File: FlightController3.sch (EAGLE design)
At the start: 43 parts, among them U1 NUCLEO_L432KC

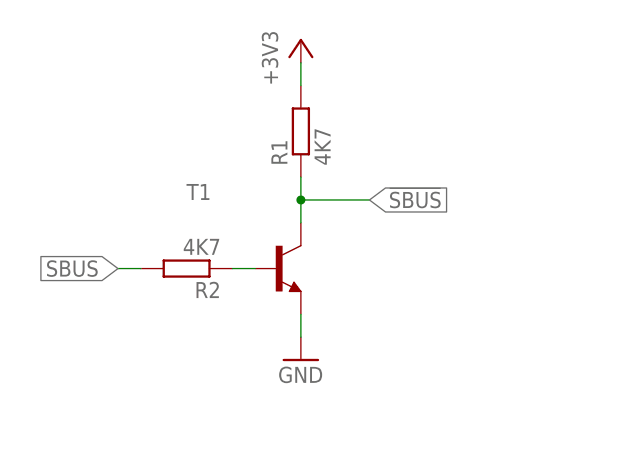
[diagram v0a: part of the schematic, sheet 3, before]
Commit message: sbus inverter spice setup
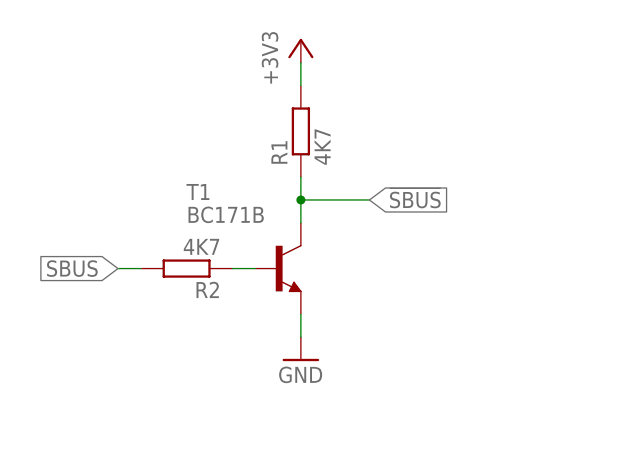
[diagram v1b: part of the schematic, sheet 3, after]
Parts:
- MF1: SPICEPREFIX (none) -> X
- R1, R2: SPICEPREFIX (none) -> R
- T1: value (none) -> BC171B; SPICEMODEL (none) -> BC171B; SPICEPREFIX (none) -> Q
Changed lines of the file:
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@@
 <part name="P+2" library="supply1" library_urn="urn:adsk.eagle:library:371" deviceset="+5V" device=""/>
 <part name="GND3" library="supply1" library_urn="urn:adsk.eagle:library:371" deviceset="GND" device=""/>
-<part name="T1" library="transistor" library_urn="urn:adsk.eagle:library:402" deviceset="*-NPN-" device="TO92"/>
-<part name="R1" library="resistor" library_urn="urn:adsk.eagle:library:348" deviceset="R-EU_" device="R0603" value="4K7"/>
-<part name="R2" library="resistor" library_urn="urn:adsk.eagle:library:348" deviceset="R-EU_" device="R0603" value="4K7"/>
+<part name="T1" library="transistor" library_urn="urn:adsk.eagle:library:402" deviceset="*-NPN-" device="TO92" value="BC171B">
+<spice>
+<pinmapping isusermap="yes" isdevicewide="no">
+<pinmap gate="G$1" pin="B" pinorder="2"/>
+<pinmap gate="G$1" pin="E" pinorder="3"/>
+<pinmap gate="G$1" pin="C" pinorder="1"/>
+</pinmapping>
+</spice>
+<attribute name="SPICEMODEL" value="BC171B"/>
+<attribute name="SPICEPREFIX" value="Q"/>
+</part>
+<part name="R1" library="resistor" library_urn="urn:adsk.eagle:library:348" deviceset="R-EU_" device="R0603" value="4K7">
+<spice>
+<pinmapping isusermap="yes" isdevicewide="yes">
+<pinmap gate="G$1" pin="2" pinorder="1"/>
+<pinmap gate="G$1" pin="1" pinorder="2"/>
+</pinmapping>
+</spice>
+<attribute name="SPICEPREFIX" value="R"/>
+</part>
+<part name="R2" library="resistor" library_urn="urn:adsk.eagle:library:348" deviceset="R-EU_" device="R0603" value="4K7">
+<spice>
+<pinmapping isusermap="yes" isdevicewide="yes">
+<pinmap gate="G$1" pin="2" pinorder="1"/>
+<pinmap gate="G$1" pin="1" pinorder="2"/>
+</pinmapping>
+</spice>
+<attribute name="SPICEPREFIX" value="R"/>
+</part>
 <part name="+3V3" library="supply1" library_urn="urn:adsk.eagle:library:371" deviceset="+3V3" device=""/>
 <part name="GND6" library="supply1" library_urn="urn:adsk.eagle:library:371" deviceset="GND" device=""/>
 <part name="INS1" library="1_Robo-Lib" deviceset="BNO055-BREAKOUT" device="" value="BNO055"/>
 <part name="GND7" library="supply1" library_urn="urn:adsk.eagle:library:371" deviceset="GND" device=""/>
-<part name="MF1" library="BSN20_215" deviceset="BSN20,215" device=""/>
+<part name="MF1" library="BSN20_215" deviceset="BSN20,215" device="">
+<attribute name="SPICEPREFIX" value="X"/>
+</part>
 <part name="MF2" library="BSN20_215" deviceset="BSN20,215" device=""/>
 <part name="R3" library="resistor" library_urn="urn:adsk.eagle:library:348" deviceset="R-EU_" device="R0603" value="4K7"/>
@@
 with this version.
 </note>
+<note version="8.4" severity="warning">
+Since Version 8.4, EAGLE supports properties for SPICE simulation.
+Probes in schematics and SPICE mapping objects found in parts and library devices
+will not be understood with this version. Update EAGLE to the latest version
+for full support of SPICE simulation.
+</note>
 </compatibility>

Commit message: i2c level shifting simulation setup
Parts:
- MF1: SPICEMODEL (none) -> BSN20
- MF2: SPICEMODEL (none) -> BSN20; SPICEPREFIX (none) -> X
- R3, R4, R5, R6: SPICEPREFIX (none) -> R
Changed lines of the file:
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@@
 <part name="GND7" library="supply1" library_urn="urn:adsk.eagle:library:371" deviceset="GND" device=""/>
 <part name="MF1" library="BSN20_215" deviceset="BSN20,215" device="">
+<spice>
+<pinmapping isusermap="yes" isdevicewide="no">
+<pinmap gate="G$1" pin="D" pinorder="1"/>
+<pinmap gate="G$1" pin="S" pinorder="3"/>
+<pinmap gate="G$1" pin="G" pinorder="2"/>
+</pinmapping>
+</spice>
+<attribute name="SPICEMODEL" value="BSN20"/>
 <attribute name="SPICEPREFIX" value="X"/>
 </part>
-<part name="MF2" library="BSN20_215" deviceset="BSN20,215" device=""/>
-<part name="R3" library="resistor" library_urn="urn:adsk.eagle:library:348" deviceset="R-EU_" device="R0603" value="4K7"/>
-<part name="R4" library="resistor" library_urn="urn:adsk.eagle:library:348" deviceset="R-EU_" device="R0603" value="4K7"/>
-<part name="R5" library="resistor" library_urn="urn:adsk.eagle:library:348" deviceset="R-EU_" device="R0603" value="4K7"/>
-<part name="R6" library="resistor" library_urn="urn:adsk.eagle:library:348" deviceset="R-EU_" device="R0603" value="4K7"/>
+<part name="MF2" library="BSN20_215" deviceset="BSN20,215" device="">
+<spice>
+<pinmapping isusermap="yes" isdevicewide="no">
+<pinmap gate="G$1" pin="D" pinorder="1"/>
+<pinmap gate="G$1" pin="S" pinorder="3"/>
+<pinmap gate="G$1" pin="G" pinorder="2"/>
+</pinmapping>
+</spice>
+<attribute name="SPICEMODEL" value="BSN20"/>
+<attribute name="SPICEPREFIX" value="X"/>
+</part>
+<part name="R3" library="resistor" library_urn="urn:adsk.eagle:library:348" deviceset="R-EU_" device="R0603" value="4K7">
+<spice>
+<pinmapping isusermap="yes" isdevicewide="yes">
+<pinmap gate="G$1" pin="2" pinorder="1"/>
+<pinmap gate="G$1" pin="1" pinorder="2"/>
+</pinmapping>
+</spice>
+<attribute name="SPICEPREFIX" value="R"/>
+</part>
+<part name="R4" library="resistor" library_urn="urn:adsk.eagle:library:348" deviceset="R-EU_" device="R0603" value="4K7">
+<spice>
+<pinmapping isusermap="yes" isdevicewide="yes">
+<pinmap gate="G$1" pin="2" pinorder="1"/>
+<pinmap gate="G$1" pin="1" pinorder="2"/>
+</pinmapping>
+</spice>
+<attribute name="SPICEPREFIX" value="R"/>
+</part>
+<part name="R5" library="resistor" library_urn="urn:adsk.eagle:library:348" deviceset="R-EU_" device="R0603" value="4K7">
+<spice>
+<pinmapping isusermap="yes" isdevicewide="yes">
+<pinmap gate="G$1" pin="2" pinorder="1"/>
+<pinmap gate="G$1" pin="1" pinorder="2"/>
+</pinmapping>
+</spice>
+<attribute name="SPICEPREFIX" value="R"/>
+</part>
+<part name="R6" library="resistor" library_urn="urn:adsk.eagle:library:348" deviceset="R-EU_" device="R0603" value="4K7">
+<spice>
+<pinmapping isusermap="yes" isdevicewide="yes">
+<pinmap gate="G$1" pin="2" pinorder="1"/>
+<pinmap gate="G$1" pin="1" pinorder="2"/>
+</pinmapping>
+</spice>
+<attribute name="SPICEPREFIX" value="R"/>
+</part>
 <part name="+3V5" library="supply1" library_urn="urn:adsk.eagle:library:371" deviceset="+3V3" device=""/>
 <part name="P+4" library="supply1" library_urn="urn:adsk.eagle:library:371" deviceset="+5V" device=""/>

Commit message: power led simulation setup
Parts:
- LED1, LED2: SPICEMODEL (none) -> SMLD12U8W; SPICEPREFIX (none) -> D
- R7, R8: SPICEPREFIX (none) -> R
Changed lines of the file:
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@@
 <part name="JP1" library="pinhead" library_urn="urn:adsk.eagle:library:325" deviceset="PINHD-1X2" device="" value="RESET"/>
 <part name="GND8" library="supply1" library_urn="urn:adsk.eagle:library:371" deviceset="GND" device=""/>
-<part name="LED1" library="led" library_urn="urn:adsk.eagle:library:259" deviceset="LED" device="SML0603" value="5V"/>
-<part name="LED2" library="led" library_urn="urn:adsk.eagle:library:259" deviceset="LED" device="SML0603" value="3V3"/>
+<part name="LED1" library="led" library_urn="urn:adsk.eagle:library:259" deviceset="LED" device="SML0603" value="5V">
+<spice>
+<pinmapping isusermap="yes" isdevicewide="no">
+<pinmap gate="G$1" pin="A" pinorder="1"/>
+<pinmap gate="G$1" pin="C" pinorder="2"/>
+</pinmapping>
+</spice>
+<attribute name="SPICEMODEL" value="SMLD12U8W"/>
+<attribute name="SPICEPREFIX" value="D"/>
+</part>
+<part name="LED2" library="led" library_urn="urn:adsk.eagle:library:259" deviceset="LED" device="SML0603" value="3V3">
+<spice>
+<pinmapping isusermap="yes" isdevicewide="no">
+<pinmap gate="G$1" pin="A" pinorder="1"/>
+<pinmap gate="G$1" pin="C" pinorder="2"/>
+</pinmapping>
+</spice>
+<attribute name="SPICEMODEL" value="SMLD12U8W"/>
+<attribute name="SPICEPREFIX" value="D"/>
+</part>
 <part name="+3V2" library="supply1" library_urn="urn:adsk.eagle:library:371" deviceset="+3V3" device=""/>
 <part name="P+8" library="supply1" library_urn="urn:adsk.eagle:library:371" deviceset="+5V" device=""/>
-<part name="R7" library="resistor" library_urn="urn:adsk.eagle:library:348" deviceset="R-EU_" device="M1206" value="110"/>
-<part name="R8" library="resistor" library_urn="urn:adsk.eagle:library:348" deviceset="R-EU_" device="M1206" value="150"/>
+<part name="R7" library="resistor" library_urn="urn:adsk.eagle:library:348" deviceset="R-EU_" device="M1206" value="110">
+<spice>
+<pinmapping isusermap="yes" isdevicewide="yes">
+<pinmap gate="G$1" pin="2" pinorder="1"/>
+<pinmap gate="G$1" pin="1" pinorder="2"/>
+</pinmapping>
+</spice>
+<attribute name="SPICEPREFIX" value="R"/>
+</part>
+<part name="R8" library="resistor" library_urn="urn:adsk.eagle:library:348" deviceset="R-EU_" device="M1206" value="150">
+<spice>
+<pinmapping isusermap="yes" isdevicewide="yes">
+<pinmap gate="G$1" pin="2" pinorder="1"/>
+<pinmap gate="G$1" pin="1" pinorder="2"/>
+</pinmapping>
+</spice>
+<attribute name="SPICEPREFIX" value="R"/>
+</part>
 <part name="GND9" library="supply1" library_urn="urn:adsk.eagle:library:371" deviceset="GND" device=""/>
 <part name="GND10" library="supply1" library_urn="urn:adsk.eagle:library:371" deviceset="GND" device=""/>

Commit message: filtering capacitor simulation setup
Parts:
- C15, C16, C17, C18: SPICEPREFIX (none) -> C
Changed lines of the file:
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@@
 <part name="GND9" library="supply1" library_urn="urn:adsk.eagle:library:371" deviceset="GND" device=""/>
 <part name="GND10" library="supply1" library_urn="urn:adsk.eagle:library:371" deviceset="GND" device=""/>
-<part name="C15" library="resistor" library_urn="urn:adsk.eagle:library:348" deviceset="C-EU" device="C1206" value="100nF"/>
-<part name="C16" library="resistor" library_urn="urn:adsk.eagle:library:348" deviceset="C-EU" device="C1206" value="100nF"/>
-<part name="C17" library="resistor" library_urn="urn:adsk.eagle:library:348" deviceset="C-EU" device="C1206" value="100nF"/>
-<part name="C18" library="resistor" library_urn="urn:adsk.eagle:library:348" deviceset="C-EU" device="C1206" value="100nF"/>
+<part name="C15" library="resistor" library_urn="urn:adsk.eagle:library:348" deviceset="C-EU" device="C1206" value="100nF">
+<spice>
+<pinmapping isusermap="yes" isdevicewide="yes">
+<pinmap gate="G$1" pin="2" pinorder="2"/>
+<pinmap gate="G$1" pin="1" pinorder="1"/>
+</pinmapping>
+</spice>
+<attribute name="SPICEPREFIX" value="C"/>
+</part>
+<part name="C16" library="resistor" library_urn="urn:adsk.eagle:library:348" deviceset="C-EU" device="C1206" value="100nF">
+<spice>
+<pinmapping isusermap="yes" isdevicewide="yes">
+<pinmap gate="G$1" pin="2" pinorder="2"/>
+<pinmap gate="G$1" pin="1" pinorder="1"/>
+</pinmapping>
+</spice>
+<attribute name="SPICEPREFIX" value="C"/>
+</part>
+<part name="C17" library="resistor" library_urn="urn:adsk.eagle:library:348" deviceset="C-EU" device="C1206" value="100nF">
+<spice>
+<pinmapping isusermap="yes" isdevicewide="yes">
+<pinmap gate="G$1" pin="2" pinorder="2"/>
+<pinmap gate="G$1" pin="1" pinorder="1"/>
+</pinmapping>
+</spice>
+<attribute name="SPICEPREFIX" value="C"/>
+</part>
+<part name="C18" library="resistor" library_urn="urn:adsk.eagle:library:348" deviceset="C-EU" device="C1206" value="100nF">
+<spice>
+<pinmapping isusermap="yes" isdevicewide="yes">
+<pinmap gate="G$1" pin="2" pinorder="2"/>
+<pinmap gate="G$1" pin="1" pinorder="1"/>
+</pinmapping>
+</spice>
+<attribute name="SPICEPREFIX" value="C"/>
+</part>
 <part name="P+10" library="supply1" library_urn="urn:adsk.eagle:library:371" deviceset="+5V" device=""/>
 <part name="P+11" library="supply1" library_urn="urn:adsk.eagle:library:371" deviceset="+5V" device=""/>

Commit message: nucleo simulation setup
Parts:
- U1: SPICEMODEL (none) -> NUCLEO; SPICEPREFIX (none) -> X
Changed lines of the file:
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@@
 <part name="+3V5" library="supply1" library_urn="urn:adsk.eagle:library:371" deviceset="+3V3" device=""/>
 <part name="P+4" library="supply1" library_urn="urn:adsk.eagle:library:371" deviceset="+5V" device=""/>
-<part name="U1" library="NUCLEO" deviceset="NUCLEO_L432KC" device=""/>
+<part name="U1" library="NUCLEO" deviceset="NUCLEO_L432KC" device="">
+<spice>
+<pinmapping isusermap="yes" isdevicewide="no">
+<pinmap gate="G$1" pin="D3" pinorder="4"/>
+<pinmap gate="G$1" pin="A3" pinorder="16"/>
+<pinmap gate="G$1" pin="D6" pinorder="7"/>
+<pinmap gate="G$1" pin="D12/SDA3" pinorder="11"/>
+<pinmap gate="G$1" pin="VIN" pinorder="21"/>
+<pinmap gate="G$1" pin="A5" pinorder="18"/>
+<pinmap gate="G$1" pin="A6/SCL3" pinorder="19"/>
+<pinmap gate="G$1" pin="!RST" pinorder="26"/>
+<pinmap gate="G$1" pin="A1" pinorder="14"/>
+<pinmap gate="G$1" pin="D0/SCL1/RX1" pinorder="1"/>
+<pinmap gate="G$1" pin="D2" pinorder="3"/>
+<pinmap gate="G$1" pin="GND" pinorder="22"/>
+<pinmap gate="G$1" pin="A4" pinorder="17"/>
+<pinmap gate="G$1" pin="D13" pinorder="12"/>
+<pinmap gate="G$1" pin="+5V" pinorder="23"/>
+<pinmap gate="G$1" pin="D1/SDA1/TX1" pinorder="2"/>
+<pinmap gate="G$1" pin="A0" pinorder="13"/>
+<pinmap gate="G$1" pin="+3V3" pinorder="24"/>
+<pinmap gate="G$1" pin="D4/SDA1/RX1" pinorder="5"/>
+<pinmap gate="G$1" pin="A2/RX2" pinorder="15"/>
+<pinmap gate="G$1" pin="D5/SCL1/TX1" pinorder="6"/>
+<pinmap gate="G$1" pin="A7/TX2" pinorder="20"/>
+<pinmap gate="G$1" pin="D10" pinorder="9"/>
+<pinmap gate="G$1" pin="D9" pinorder="8"/>
+<pinmap gate="G$1" pin="AREF" pinorder="25"/>
+<pinmap gate="G$1" pin="D11" pinorder="10"/>
+</pinmapping>
+</spice>
+<attribute name="SPICEMODEL" value="NUCLEO"/>
+<attribute name="SPICEPREFIX" value="X"/>
+</part>
 <part name="GND4" library="supply1" library_urn="urn:adsk.eagle:library:371" deviceset="GND" device=""/>
 <part name="P+3" library="supply1" library_urn="urn:adsk.eagle:library:371" deviceset="+5V" device=""/>

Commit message: EEPROM simulation setup
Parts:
- U$3: SPICEMODEL (none) -> AT24C16C; SPICEPREFIX (none) -> X
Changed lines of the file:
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@@
 <part name="+3V7" library="supply1" library_urn="urn:adsk.eagle:library:371" deviceset="+3V3" device=""/>
 <part name="SJ1" library="jumper" library_urn="urn:adsk.eagle:library:252" deviceset="SJ2W" device=""/>
-<part name="U$3" library="JonasLib" deviceset="AT24C16C" device=""/>
+<part name="U$3" library="JonasLib" deviceset="AT24C16C" device="">
+<spice>
+<pinmapping isusermap="yes" isdevicewide="no">
+<pinmap gate="G$1" pin="SDA" pinorder="2"/>
+<pinmap gate="G$1" pin="VCC" pinorder="4"/>
+<pinmap gate="G$1" pin="SCL" pinorder="3"/>
+<pinmap gate="G$1" pin="WP" pinorder="1"/>
+<pinmap gate="G$1" pin="GND" pinorder="5"/>
+</pinmapping>
+</spice>
+<attribute name="SPICEMODEL" value="AT24C16C"/>
+<attribute name="SPICEPREFIX" value="X"/>
+</part>
 <part name="P+9" library="supply1" library_urn="urn:adsk.eagle:library:371" deviceset="+5V" device=""/>
 <part name="GND16" library="supply1" library_urn="urn:adsk.eagle:library:371" deviceset="GND" device=""/>
